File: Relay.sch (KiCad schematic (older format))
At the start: 7 parts

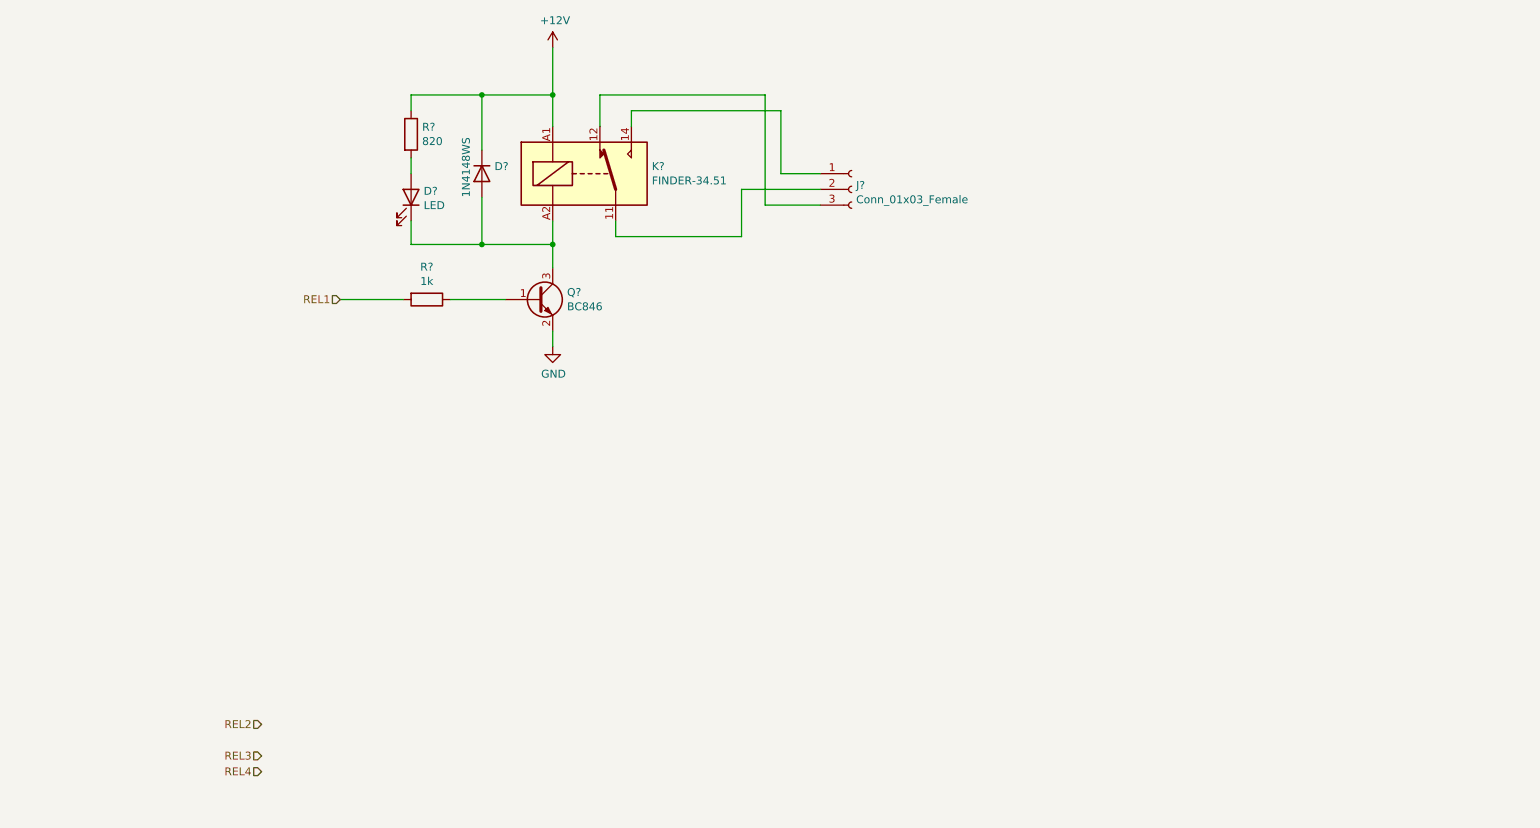
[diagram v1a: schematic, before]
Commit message: add SDcard, OneWire, Batt, analog out, digital out
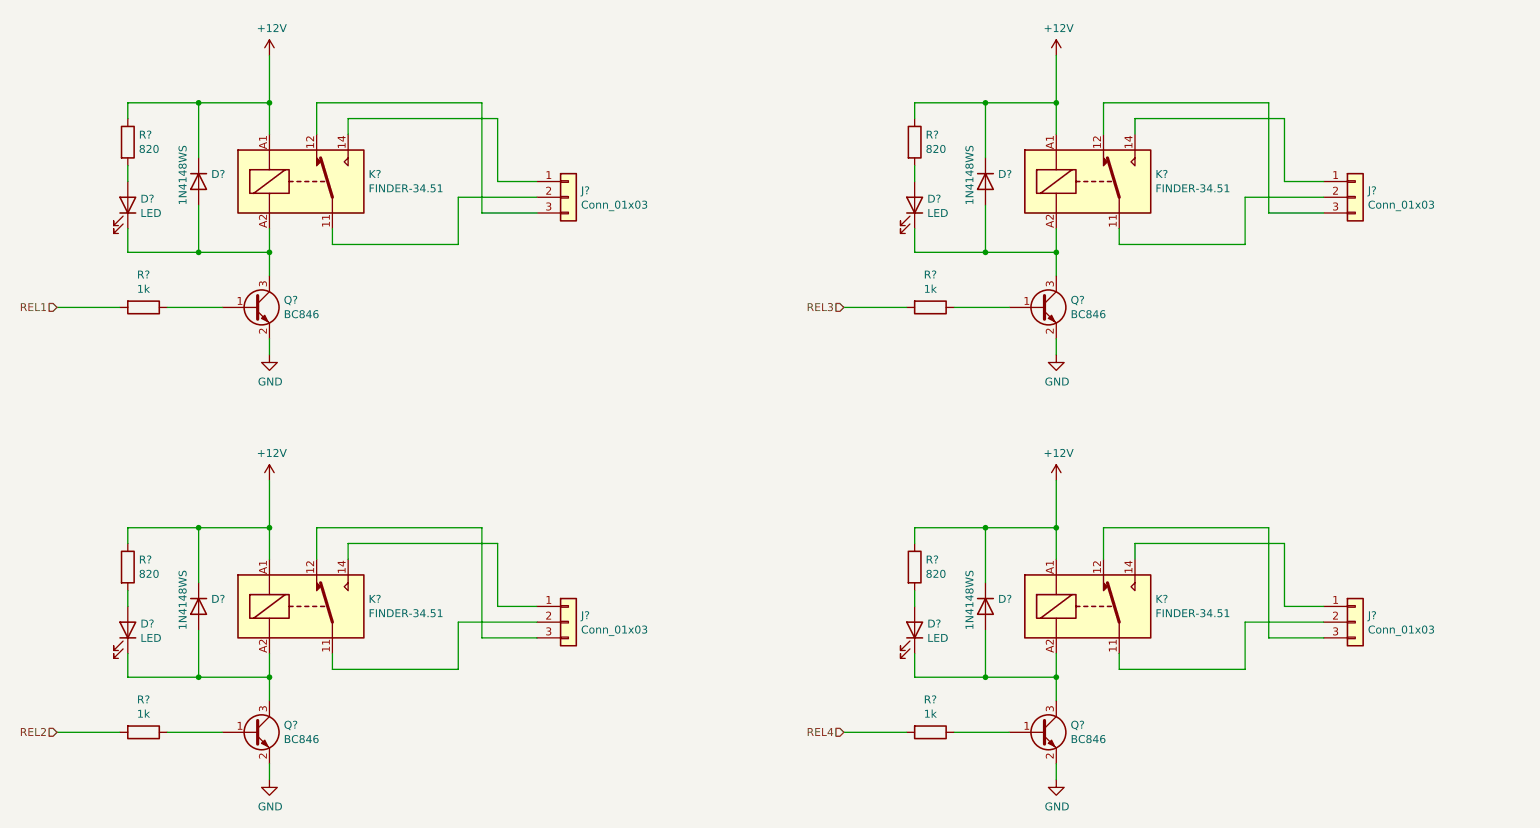
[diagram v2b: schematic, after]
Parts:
- removed J?: Conn_01x03_Female, symbol Connector:Conn_01x03_Female
- added D? (x3): 1N4148WS, Diode_SMD:D_SOD-323, symbol Diode:1N4148WS
- added D? (x3): LED, symbol Device:LED
- added J? (x4): Conn_01x03, symbol Connector_Generic:Conn_01x03
- added K? (x3): FINDER-34.51, Relay_THT:Relay_SPDT_Finder_34.51_Vertical, symbol Relay:FINDER-34.51
- added Q? (x3): BC846, Package_TO_SOT_SMD:SOT-23, symbol Transistor_BJT:BC846
- added R? (x3): 1k, symbol AR2ISS:R
- added R? (x3): 820, symbol AR2ISS:R
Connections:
- net +12V: now also D?.1 (K), D?.1 (K), D?.1 (K), K?.A1, K?.A1, K?.A1, R?.1, R?.1, R?.1
- net GND: now also Q?.2 (E), Q?.2 (E), Q?.2 (E)
- net REL2: now also R?.2
- net REL3: now also R?.2
- net REL4: now also R?.2
- net at K?.11: now also J?.2 (Pin_2)
- net at K?.12: now also J?.3 (Pin_3)
- net at K?.14: now also J?.1 (Pin_1)
- new net: Q?.1 (B), R?.1 (x3)
- new net: D?.1 (K), D?.2 (A), K?.A2, Q?.3 (C) (x3)
- new net: J?.2 (Pin_2), K?.11 (x3)
- new net: J?.3 (Pin_3), K?.12 (x3)
- new net: J?.1 (Pin_1), K?.14 (x3)
- new net: D?.2 (A), R?.2 (x3)
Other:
- moved on the sheet: D?, K?, Q?, R?

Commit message: start placement
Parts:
- removed J? (x4): Conn_01x03, symbol Connector_Generic:Conn_01x03
- added J1, J2: Conn_01x06, AR2ISS:250-206, symbol Connector_Generic:Conn_01x06
- D1, D2, D5, D6: renamed from D?; footprint (none) -> LED_SMD:LED_0603_1608Metric
- R10, R11, R4, R5, R6, R7, R8, R9: renamed from R?; footprint (none) -> Resistor_SMD:R_0603_1608Metric
- gave numbers to parts that had none: 12
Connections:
- net at K1.11: now also J1.2 (Pin_2)
- net at K1.12: now also J1.3 (Pin_3)
- net at K1.14: now also J1.1 (Pin_1)
- net at K2.11: now also J1.5 (Pin_5)
- net at K2.12: now also J1.6 (Pin_6)
- net at K2.14: now also J1.4 (Pin_4)
- net at K3.11: now also J2.2 (Pin_2)
- net at K3.12: now also J2.3 (Pin_3)
- net at K3.14: now also J2.1 (Pin_1)
- net at K4.11: now also J2.5 (Pin_5)
- net at K4.12: now also J2.6 (Pin_6)
- net at K4.14: now also J2.4 (Pin_4)

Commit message: placement
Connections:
- net at K1.12: now also J1.1 (Pin_1); no longer J1.3 (Pin_3)
- net at K1.14: now also J1.3 (Pin_3); no longer J1.1 (Pin_1)
- net at J1.4 (Pin_4): now also K2.12; no longer K2.14
- net at J1.6 (Pin_6): now also K2.14; no longer K2.12
- net at J2.1 (Pin_1): now also K3.12; no longer K3.14
- net at J2.3 (Pin_3): now also K3.14; no longer K3.12
- net at J2.4 (Pin_4): now also K4.12; no longer K4.14
- net at J2.6 (Pin_6): now also K4.14; no longer K4.12
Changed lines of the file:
@@
 $Descr A4 11693 8268
 encoding utf-8
-Sheet 2 21
+Sheet 2 22
 Title ""
 Date ""
@@
 	8000 4250 8000 4150
 Wire Wire Line
-	8000 4150 8950 4150
+	8000 4150 8850 4150
 Wire Wire Line
 	7800 4250 7800 4050
-Wire Wire Line
-	7800 4050 8850 4050
 $Comp
 L Device:LED D6
@@
 	3700 3150 3700 2250
 Wire Wire Line
-	4700 3050 3950 3050
-Wire Wire Line
-	4700 3250 3850 3250
-Wire Wire Line
 	4700 3450 3700 3450
 Wire Wire Line
-	4700 3350 3950 3350
-Wire Wire Line
-	3950 3350 3950 4150
-Wire Wire Line
-	4700 3550 3850 3550
-Wire Wire Line
-	3850 3550 3850 4050
-Wire Wire Line
-	3850 1350 3850 3250
-Wire Wire Line
-	3950 1450 3950 3050
+	3850 1350 3850 3050
 Wire Wire Line
 	3700 3450 3700 4950
@@
 	9700 3150 8700 3150
 Wire Wire Line
-	9700 3050 8950 3050
-Wire Wire Line
-	9700 3250 8850 3250
+	8850 1350 8850 3050
+Wire Wire Line
+	8700 3150 8700 2250
 Wire Wire Line
 	9700 3450 8700 3450
 Wire Wire Line
-	9700 3350 8950 3350
-Wire Wire Line
-	8950 3350 8950 4150
-Wire Wire Line
-	9700 3550 8850 3550
-Wire Wire Line
-	8850 3550 8850 4050
-Wire Wire Line
-	8950 1450 8950 3050
-Wire Wire Line
-	8850 1350 8850 3250
-Wire Wire Line
-	8700 3150 8700 2250
-Wire Wire Line
 	8700 3450 8700 4950
+Wire Wire Line
+	8850 3550 8850 4150
+Wire Wire Line
+	8850 3550 9700 3550
+Wire Wire Line
+	9700 3350 8600 3350
+Wire Wire Line
+	8600 3350 8600 4050
+Wire Wire Line
+	8600 4050 7800 4050
+Wire Wire Line
+	8950 3250 9700 3250
+Wire Wire Line
+	8950 1450 8950 3250
+Wire Wire Line
+	9700 3050 8850 3050
+Wire Wire Line
+	4700 3550 3950 3550
+Wire Wire Line
+	3950 3550 3950 4150
+Wire Wire Line
+	4700 3350 3850 3350
+Wire Wire Line
+	3850 3350 3850 4050
+Wire Wire Line
+	3950 3250 4700 3250
+Wire Wire Line
+	3950 1450 3950 3250
+Wire Wire Line
+	4700 3050 3850 3050
 $EndSCHEMATC

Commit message: ready for jlc
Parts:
- D1, D2, D5, D6: value LED -> LED_R
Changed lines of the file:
@@
 P 1600 2000
 F 0 "D1" V 1639 2080 50  0000 L CNN
-F 1 "LED" V 1548 2080 50  0000 L CNN
+F 1 "LED_R" V 1548 2080 50  0000 L CNN
 F 2 "LED_SMD:LED_0603_1608Metric" H 1600 2000 50  0001 C CNN
 F 3 "~" H 1600 2000 50  0001 C CNN
@@
 P 1600 4700
 F 0 "D2" V 1639 4780 50  0000 L CNN
-F 1 "LED" V 1548 4780 50  0000 L CNN
+F 1 "LED_R" V 1548 4780 50  0000 L CNN
 F 2 "LED_SMD:LED_0603_1608Metric" H 1600 4700 50  0001 C CNN
 F 3 "~" H 1600 4700 50  0001 C CNN
@@
 P 6600 2000
 F 0 "D5" V 6639 2080 50  0000 L CNN
-F 1 "LED" V 6548 2080 50  0000 L CNN
+F 1 "LED_R" V 6548 2080 50  0000 L CNN
 F 2 "LED_SMD:LED_0603_1608Metric" H 6600 2000 50  0001 C CNN
 F 3 "~" H 6600 2000 50  0001 C CNN
@@
 P 6600 4700
 F 0 "D6" V 6639 4780 50  0000 L CNN
-F 1 "LED" V 6548 4780 50  0000 L CNN
+F 1 "LED_R" V 6548 4780 50  0000 L CNN
 F 2 "LED_SMD:LED_0603_1608Metric" H 6600 4700 50  0001 C CNN
 F 3 "~" H 6600 4700 50  0001 C CNN
